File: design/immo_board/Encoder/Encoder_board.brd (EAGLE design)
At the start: 44.5 x 14 mm, 2 parts

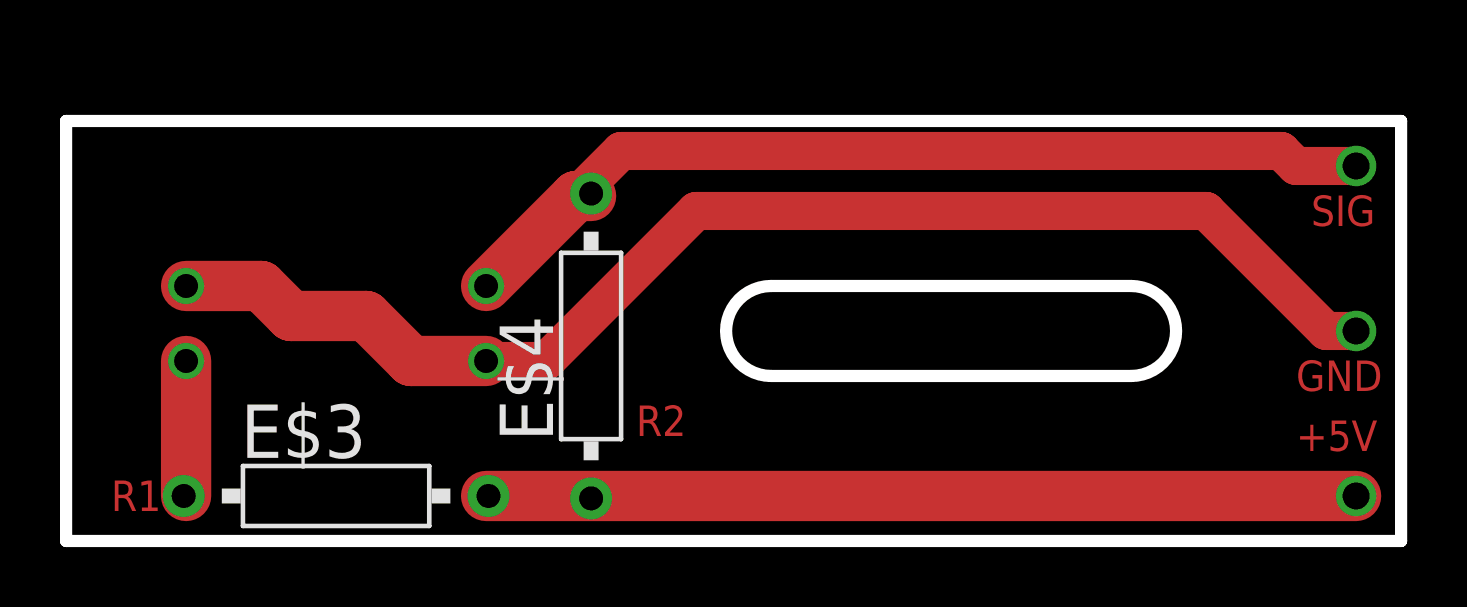
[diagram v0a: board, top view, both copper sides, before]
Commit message: Fix board and electrical scheme for Encoder, Driver, WS2812B.
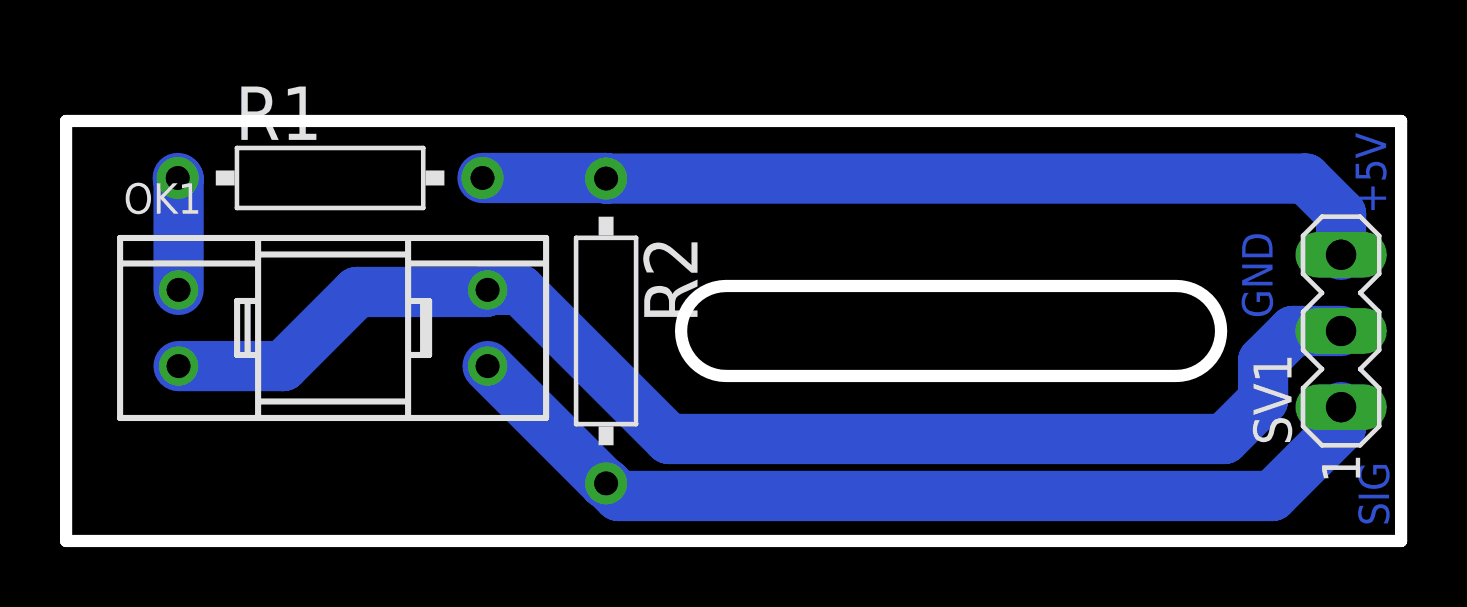
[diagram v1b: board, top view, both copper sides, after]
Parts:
- removed E$3, E$4: (no value), resistor-power:RS1/4
- added OK1: SFH9310, optocoupler:SFH9310
- added R1, R2: (no value), resistor-power:RS1/4
- added SV1: (no value), con-lstb:MA03-1
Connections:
- new net +5V: R1.2, R2.1, SV1.3
- new net GND: OK1.2, OK1.3, SV1.2
- new net N$2: OK1.1, R1.1
- new net SIG: OK1.4, R2.2, SV1.1
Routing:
- net GND: track 0.00 -> 44.1 mm
- net S$11: track 32.7 -> 0.00 mm, vias 1 -> 0
- net SIG: track 0.00 -> 31.9 mm
- net S$10: track 31.6 -> 0.00 mm, vias 1 -> 0
- net +5V: track 0.00 -> 30.5 mm
- net S$14: track 29.0 -> 0.00 mm, vias 1 -> 0
- net S$9: track 11.0 -> 0.00 mm, vias 1 -> 0
- net S$1: track 4.50 -> 0.00 mm, vias 1 -> 0
- net N$2: track 0.00 -> 3.74 mm
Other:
- outline, holes or cut-outs redrawn
- board text removed: "R1"
- board text removed: "R2"

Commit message: Fix board and electric scheme. Add capacitors.
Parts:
- R1: value (none) -> 100 Om
- R2: value (none) -> 3.3 kOm
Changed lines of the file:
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@@
 <attribute name="OC_FARNELL" value="unknown" x="-21.1" y="38.6" size="1.778" layer="27" display="off"/>
 </element>
-<element name="R1" library="resistor-power" package="RS1/4" value="" x="-21.2" y="43.6">
+<element name="R1" library="resistor-power" package="RS1/4" value="100 Om" x="-21.2" y="43.6">
 <attribute name="OC_NEWARK" value="01F7661" x="-21.2" y="43.6" size="1.778" layer="27" display="off"/>
 <attribute name="MPN" value="RRS1K0" x="-21.2" y="43.6" size="1.778" layer="27" display="off"/>
@@
 <attribute name="OC_FARNELL" value="unknown" x="-21.2" y="43.6" size="1.778" layer="27" display="off"/>
 </element>
-<element name="R2" library="resistor-power" package="RS1/4" value="" x="-12" y="38.5" rot="R270">
+<element name="R2" library="resistor-power" package="RS1/4" value="3.3 kOm" x="-12" y="38.5" rot="R270">
 <attribute name="OC_NEWARK" value="01F7661" x="-12" y="38.5" size="1.778" layer="27" rot="R270" display="off"/>
 <attribute name="MPN" value="RRS1K0" x="-12" y="38.5" size="1.778" layer="27" rot="R270" display="off"/>
